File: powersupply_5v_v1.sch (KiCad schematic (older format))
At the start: 100 parts, among them T1 TRANSFO2, U1 LM7805, U2 LM7905

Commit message: annoated schematic and added labels
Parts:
- removed C1, C2, C3, C4: 1000uF, symbol CP
- removed C5, C6: 0.01uF, symbol C_Small
- removed C7, C8: 1.0uF, symbol C_Small
- removed C? (x8): C_Small, symbol C_Small
- removed C? (x2): 2200uF, symbol CP
- removed C? (x4): 10nF, symbol C_Small
- removed C? (x4): 100nF, symbol C_Small
- removed C? (x2): 470uF, symbol CP
- removed D? (x8): D, symbol D
- removed D? (x4): 1N4008, symbol D
- removed D? (x2): TVS, symbol TVS
- removed D? (x2): LED, symbol LED
- removed F? (x4): FUSE, symbol FUSE
- removed P? (x4): CONN_01X02, symbol CONN_01X02
- removed R? (x6): R, symbol R
- removed T? (x2): TRANSFO, symbol TRANSFO
- removed U1: LM7805, symbol LM7805
- removed U2: LM7905, symbol LM7905-RESCUE-powersupply_5v_v1
- removed U? (x2): 7805, symbol 7805
- added P1: AC_INPUT, symbol CONN_01X03
- added P2: POWER OUT, symbol CONN_01X03
- C1, C10, C11, C12, C13, C14, C15, C16, C17, C18, C2, C3, C4, C5, C6, C7, C8, C9: renamed from C?; MANUFACTURER_PART (none) -> empty
- D1, D2: value D -> MUR860G; MANUFACTURER_PART (none) -> empty
- D10, D5, D6, D7, D8, D9: renamed from D?; MANUFACTURER_PART (none) -> empty
- D3: renamed from D4; value D -> MUR860G; MANUFACTURER_PART (none) -> empty
- D4: renamed from D3; value D -> MUR860G; MANUFACTURER_PART (none) -> empty
- F1, F2, F3: renamed from F?; MANUFACTURER_PART (none) -> empty
- R1, R2: renamed from R?; MANUFACTURER_PART (none) -> empty
- T1: MANUFACTURER_PART (none) -> empty
- U1: renamed from U?; value 7805 -> LM7805CT/NOPB; MANUFACTURER_PART (none) -> empty
- U2: renamed from U?; value LM7905 -> LM7905CT/NOPB; MANUFACTURER_PART (none) -> empty
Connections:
- net labels removed: +5V, -5V, GND
- wire segments 339 -> 82
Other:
- note added: "References"
- note removed: "0V"
- note removed: "VCC"
- moved on the sheet: C1, C2, C3, C4, D1, D2, D3, D4, F1, T1

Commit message: bunch of stuff wasn't commited...
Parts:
- added U?: V+, symbol V+
- added U?: V-, symbol V-
- C1, C11, C12, C13, C14, C2, C3, C4: footprint (none) -> Capacitors_ThroughHole:C_Disc_D7.5_P5
- C10, C15, C16, C9: footprint (none) -> Capacitors_ThroughHole:C_Disc_D6_P5
- C17, C18: footprint (none) -> Capacitors_Elko_ThroughHole:Elko_vert_11.5x8mm_RM3.5
- C5, C6, C7, C8: footprint (none) -> w_capacitors:CP_18x16mm
- D1, D2, D3, D4: footprint (none) -> Diodes_ThroughHole:Diode_TO-220_Vertical
- D10, D5, D6, D9: footprint (none) -> Diodes_ThroughHole:Diode_DO-41_SOD81_Horizontal_RM10
- D7, D8: footprint (none) -> LEDs:LED-5MM
- F1, F2, F3: footprint (none) -> Fuse_Holders_and_Fuses:Fuseholder6x32_Horiz_Open_Schurter0031-8002
- P1, P2: footprint (none) -> w_conn_screw:mstbva_2,5%2f3-g-5,08
- R1, R2: footprint (none) -> Resistors_ThroughHole:Resistor_Horizontal_RM10mm
- T1: footprint (none) -> Transformers_SMPS_ThroughHole:ETD29_13Pin_Horizontal_EPCOS-B66359A1013T
- U1, U2: footprint (none) -> w_to:to220_std_14cw
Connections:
- net labels added: GND, GNDPWR
- wire segments 82 -> 87

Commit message: added footprint that was screwed up
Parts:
- removed U2: LM7905CT/NOPB, w_to:to220_std_14cw, symbol LM7905-RESCUE-powersupply_5v_v1
- added U?: 7905, symbol 7905
- U1: symbol 7805 -> 7805-RESCUE-powersupply_5v_v1
- gave numbers to parts that had none: 2
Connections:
- wire segments 87 -> 144
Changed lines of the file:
@@
 http://elinux.org/RPi_5V_PSU_construction
-$Comp
-L LM7905-RESCUE-powersupply_5v_v1 U2
-U 1 1 55CE5E33
-P 4850 6075
-F 0 "U2" H 5000 5880 60  0000 C CNN
-F 1 "LM7905CT/NOPB" H 4850 6275 60  0000 C CNN
-F 2 "w_to:to220_std_14cw" H 4850 6075 60  0001 C CNN
-F 3 "" H 4850 6075 60  0000 C CNN
-F 4 "empty" H 4850 6075 60  0000 C CNN "MANUFACTURER_PART"
-	1    4850 6075
-	1    0    0    -1
-$EndComp
 $Comp
 L FUSE F1
@@
 $EndComp
 $Comp
-L 7805 U1
+L 7805-RESCUE-powersupply_5v_v1 U1
 U 1 1 55CEF6E0
 P 4850 4600
@@
 References
 $Comp
-L GNDPWR #PWR?
+L GNDPWR #PWR02
 U 1 1 563A2E33
 P 1600 5395
-F 0 "#PWR?" H 1600 5195 50  0001 C CNN
+F 0 "#PWR02" H 1600 5195 50  0001 C CNN
 F 1 "GNDPWR" H 1600 5265 50  0000 C CNN
 F 2 "" H 1600 5345 60  0000 C CNN
@@
 $EndComp
 $Comp
-L V+ U?
+L V+ U3
 U 1 1 563A33A0
 P 1585 4360
-F 0 "U?" H 1555 4385 60  0000 C CNN
+F 0 "U3" H 1555 4385 60  0000 C CNN
 F 1 "V+" H 1555 4385 60  0000 C CNN
 F 2 "" H 1555 4385 60  0000 C CNN
@@
 $EndComp
 $Comp
-L V- U?
+L V- U4
 U 1 1 563A3C79
 P 1585 5870
-F 0 "U?" H 1555 5895 60  0000 C CNN
+F 0 "U4" H 1555 5895 60  0000 C CNN
 F 1 "V-" H 1555 5895 60  0000 C CNN
 F 2 "" H 1555 5895 60  0000 C CNN
@@
 $EndComp
 Wire Wire Line
-	3275 2400 4275 2400
-Wire Wire Line
-	4150 2900 4150 3050
-Wire Wire Line
-	3525 3050 4275 3050
-Wire Wire Line
-	4700 3050 4575 3050
-Wire Wire Line
-	4700 2900 4700 3600
-Wire Wire Line
-	4700 2400 4700 2600
-Wire Wire Line
-	4575 2400 5450 2400
+	3275 2400 4150 2400
+Wire Wire Line
+	4150 2400 4225 2400
+Wire Wire Line
+	4225 2400 4275 2400
+Wire Wire Line
+	4150 2900 4150 2950
+Wire Wire Line
+	4150 2950 4150 3050
+Wire Wire Line
+	3525 3050 4150 3050
+Wire Wire Line
+	4150 3050 4225 3050
+Wire Wire Line
+	4225 3050 4275 3050
+Wire Wire Line
+	4700 3050 4600 3050
+Wire Wire Line
+	4600 3050 4575 3050
+Wire Wire Line
+	4700 2900 4700 2950
+Wire Wire Line
+	4700 2950 4700 3050
+Wire Wire Line
+	4700 3050 4700 3600
+Wire Wire Line
+	4700 2400 4700 2500
+Wire Wire Line
+	4700 2500 4700 2600
+Wire Wire Line
+	4575 2400 4600 2400
+Wire Wire Line
+	4600 2400 4700 2400
+Wire Wire Line
+	4700 2400 5450 2400
 Wire Wire Line
 	4700 3600 3625 3600
@@
 	3625 3200 3625 3600
 Wire Wire Line
-	4150 2400 4150 2600
-Wire Wire Line
-	3275 2700 3275 2900
+	4150 2400 4150 2525
+Wire Wire Line
+	4150 2525 4150 2600
+Wire Wire Line
+	3275 2700 3275 2800
+Wire Wire Line
+	3275 2800 3275 2900
 Wire Wire Line
 	3275 2800 3450 2800
@@
 	1425 3100 2475 3100
 Wire Wire Line
-	1425 4550 4450 4550
-Wire Wire Line
-	1375 5350 9350 5350
-Wire Wire Line
-	2550 5125 2550 5550
+	1425 4550 1700 4550
+Wire Wire Line
+	1700 4550 2550 4550
+Wire Wire Line
+	2550 4550 2950 4550
+Wire Wire Line
+	2950 4550 3500 4550
+Wire Wire Line
+	3500 4550 3950 4550
+Wire Wire Line
+	3950 4550 4450 4550
+Wire Wire Line
+	1375 5350 1400 5350
+Wire Wire Line
+	1400 5350 1600 5350
+Wire Wire Line
+	1600 5350 2550 5350
+Wire Wire Line
+	2550 5350 2950 5350
+Wire Wire Line
+	2950 5350 3500 5350
+Wire Wire Line
+	3500 5350 3950 5350
+Wire Wire Line
+	3950 5350 4850 5350
+Wire Wire Line
+	4850 5350 6075 5350
+Wire Wire Line
+	6075 5350 6475 5350
+Wire Wire Line
+	6475 5350 6900 5350
+Wire Wire Line
+	6900 5350 7275 5350
+Wire Wire Line
+	7275 5350 7675 5350
+Wire Wire Line
+	7675 5350 8400 5350
+Wire Wire Line
+	8400 5350 9350 5350
+Wire Wire Line
+	2550 5125 2550 5350
+Wire Wire Line
+	2550 5350 2550 5550
 Wire Wire Line
 	2550 6025 2550 5850
 Connection ~ 2550 5350
 Wire Wire Line
-	2950 5125 2950 5550
+	2950 5125 2950 5350
+Wire Wire Line
+	2950 5350 2950 5550
 Connection ~ 2950 5350
 Wire Wire Line
@@
 Connection ~ 1400 5350
 Wire Wire Line
-	1425 6025 4450 6025
+	1425 6025 1580 6025
+Wire Wire Line
+	1580 6025 2550 6025
+Wire Wire Line
+	2550 6025 2950 6025
+Wire Wire Line
+	2950 6025 3500 6025
+Wire Wire Line
+	3500 6025 3950 6025
+Wire Wire Line
+	3950 6025 4450 6025
 Wire Wire Line
 	4300 2125 4225 2125
@@
 Connection ~ 3500 4550
 Wire Wire Line
-	3500 5075 3500 5600
+	3500 5075 3500 5350
+Wire Wire Line
+	3500 5350 3500 5600
 Connection ~ 3500 5350
 Wire Wire Line
@@
 	3950 4550 3950 4875
 Wire Wire Line
-	3950 5075 3950 5600
+	3950 5075 3950 5350
+Wire Wire Line
+	3950 5350 3950 5600
 Connection ~ 3950 5350
 Wire Wire Line
@@
 	6075 4850 6075 4550
 Wire Wire Line
-	5250 4550 7900 4550
+	5250 4550 6075 4550
+Wire Wire Line
+	6075 4550 6475 4550
+Wire Wire Line
+	6475 4550 6900 4550
+Wire Wire Line
+	6900 4550 7275 4550
+Wire Wire Line
+	7275 4550 7675 4550
+Wire Wire Line
+	7675 4550 7900 4550
 Wire Wire Line
 	6475 4550 6475 4850
@@
 Connection ~ 6475 4550
 Wire Wire Line
-	6075 5050 6075 5550
-Wire Wire Line
-	6475 5050 6475 5575
-Wire Wire Line
-	6900 5100 6900 5525
+	6075 5050 6075 5350
+Wire Wire Line
+	6075 5350 6075 5550
+Wire Wire Line
+	6475 5050 6475 5350
+Wire Wire Line
+	6475 5350 6475 5575
+Wire Wire Line
+	6900 5100 6900 5350
+Wire Wire Line
+	6900 5350 6900 5525
 Wire Wire Line
 	7275 4550 7275 4600
@@
 	8400 4550 8400 4775
 Wire Wire Line
-	8400 5075 8400 5550
+	8400 5075 8400 5350
+Wire Wire Line
+	8400 5350 8400 5550
 Wire Wire Line
 	8400 4550 9375 4550
@@
 	7675 5000 7675 5025
 Wire Wire Line
-	7675 5325 7675 5400
+	7675 5325 7675 5350
+Wire Wire Line
+	7675 5350 7675 5400
 Connection ~ 7675 5350
 Connection ~ 3950 6025
@@
 	8400 6025 8400 5850
 Wire Wire Line
-	5250 6025 7900 6025
+	5250 6025 6075 6025
+Wire Wire Line
+	6075 6025 6475 6025
+Wire Wire Line
+	6475 6025 6900 6025
+Wire Wire Line
+	6900 6025 7275 6025
+Wire Wire Line
+	7275 6025 7675 6025
+Wire Wire Line
+	7675 6025 7900 6025
 Wire Wire Line
 	8400 6025 9350 6025
@@
 	1725 3475 1725 3525
 Wire Wire Line
-	4850 4850 4850 5825
+	4850 4850 4850 5350
+Wire Wire Line
+	4850 5350 4850 5725
 Connection ~ 4850 5350
 Wire Wire Line
@@
 Connection ~ 5250 6025
 Connection ~ 4450 6025
-Connection ~ 4850 5825
+Connection ~ 4850 5725
 Connection ~ 4850 4850
 Connection ~ 5250 4550
@@
 Connection ~ 1580 6025
 Wire Wire Line
-	1600 5255 1600 5395
+	1600 5255 1600 5350
+Wire Wire Line
+	1600 5350 1600 5395
 Connection ~ 1600 5350
 Text Label 1615 5255 0    60   ~ 0
@@
 Wire Wire Line
 	1600 5255 1615 5255
+$Comp
+L 7905 U?
+U 1 1 563AD8EE
+P 4850 5975
+F 0 "U?" H 5000 5780 60  0000 C CNN
+F 1 "7905" H 4850 6175 60  0000 C CNN
+F 2 "" H 4850 5975 60  0000 C CNN
+F 3 "" H 4850 5975 60  0000 C CNN
+	1    4850 5975
+	1    0    0    1
+$EndComp
 $EndSCHEMATC

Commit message: added some symbol stuff
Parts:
- removed U3: V+, symbol V+
- removed U4: V-, symbol V-
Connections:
- wire segments 144 -> 90
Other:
- moved on the sheet: T1

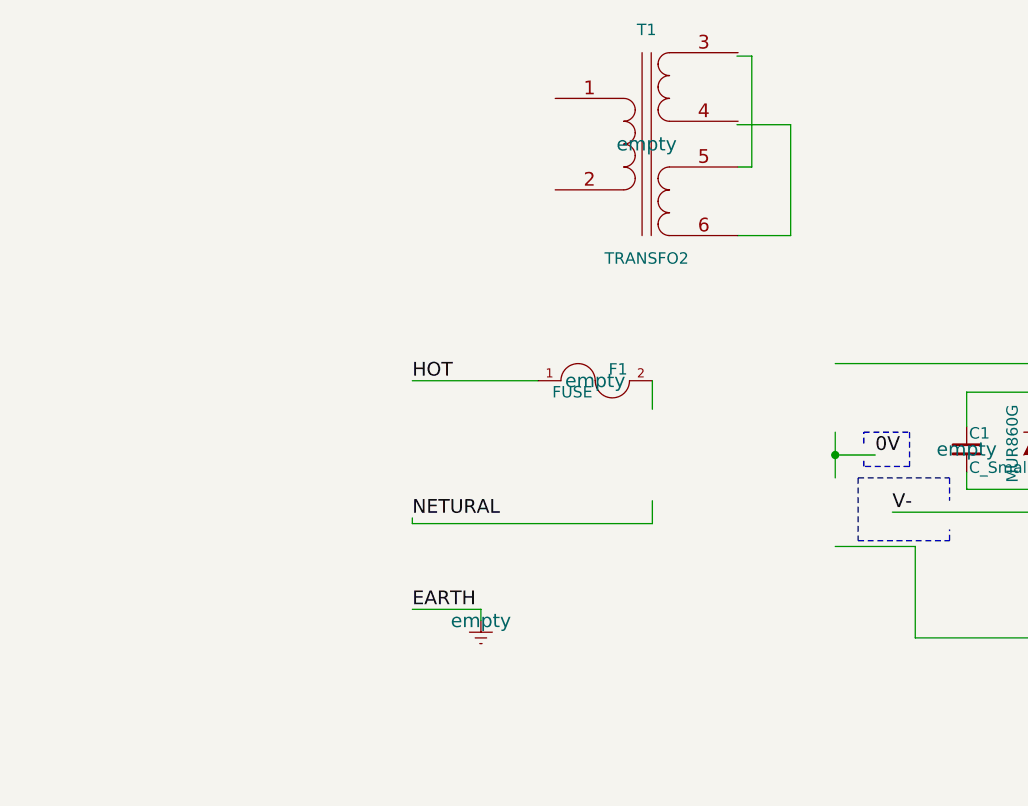
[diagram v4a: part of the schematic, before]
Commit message: trying to get this hammond transformer footprint made
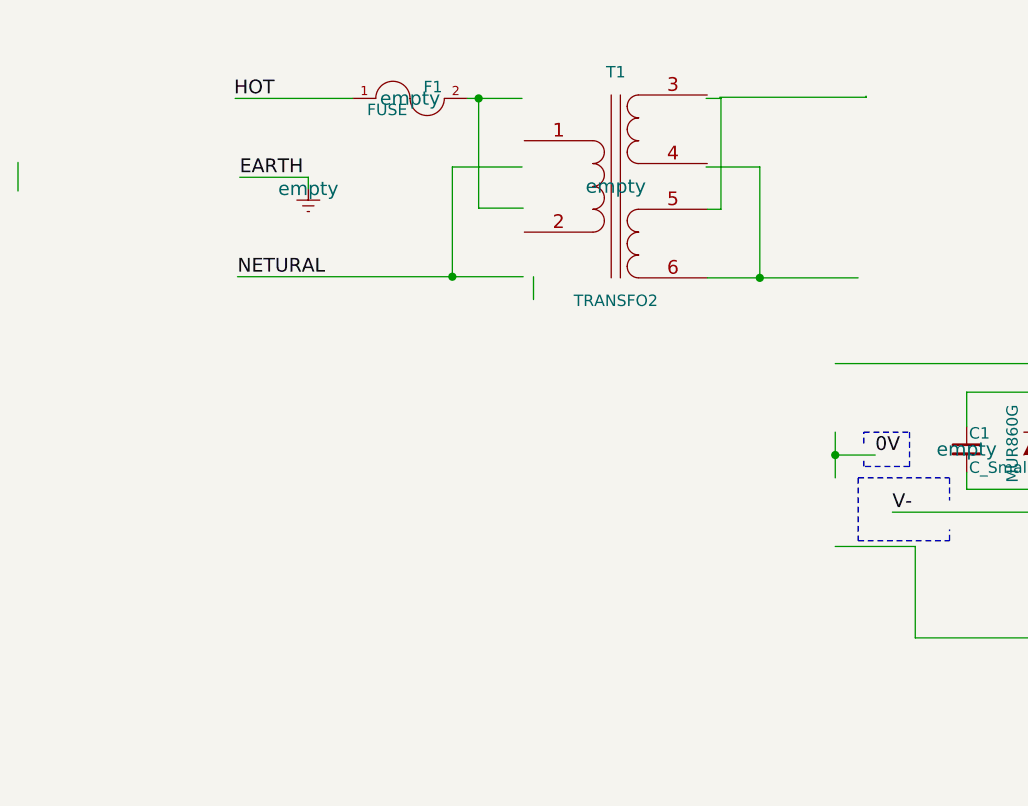
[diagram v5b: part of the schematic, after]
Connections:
- wire segments 90 -> 96
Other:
- moved on the sheet: F1, T1
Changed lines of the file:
@@
 L TRANSFO2 T1
 U 1 1 55CBB17B
-P 2450 1440
-F 0 "T1" H 2450 1940 50  0000 C CNN
-F 1 "TRANSFO2" H 2450 940 50  0000 C CNN
-F 2 "Transformers_SMPS_ThroughHole:ETD29_13Pin_Horizontal_EPCOS-B66359A1013T" H 2450 1440 60  0001 C CNN
-F 3 "" H 2450 1440 60  0000 C CNN
-F 4 "empty" H 2450 1440 60  0000 C CNN "MANUFACTURER_PART"
-	1    2450 1440
+P 2315 1625
+F 0 "T1" H 2315 2125 50  0000 C CNN
+F 1 "TRANSFO2" H 2315 1125 50  0000 C CNN
+F 2 "Transformers_SMPS_ThroughHole:ETD29_13Pin_Horizontal_EPCOS-B66359A1013T" H 2315 1625 60  0001 C CNN
+F 3 "" H 2315 1625 60  0000 C CNN
+F 4 "empty" H 2315 1625 60  0000 C CNN "MANUFACTURER_PART"
+	1    2315 1625
 	1    0    0    -1
 $EndComp
@@
 L Earth #PWR01
 U 1 1 55CD146C
-P 1725 3525
-F 0 "#PWR01" H 1725 3275 50  0001 C CNN
-F 1 "Earth" H 1725 3375 50  0001 C CNN
-F 2 "" H 1725 3525 60  0000 C CNN
-F 3 "" H 1725 3525 60  0000 C CNN
-F 4 "empty" H 1725 3525 60  0000 C CNN "MANUFACTURER_PART"
-	1    1725 3525
+P 970 1635
+F 0 "#PWR01" H 970 1385 50  0001 C CNN
+F 1 "Earth" H 970 1485 50  0001 C CNN
+F 2 "" H 970 1635 60  0000 C CNN
+F 3 "" H 970 1635 60  0000 C CNN
+F 4 "empty" H 970 1635 60  0000 C CNN "MANUFACTURER_PART"
+	1    970  1635
 	1    0    0    -1
 $EndComp
@@
 L FUSE F1
 U 1 1 55CE7C40
-P 2225 2475
-F 0 "F1" H 2325 2525 50  0000 C CNN
-F 1 "FUSE" H 2125 2425 50  0000 C CNN
-F 2 "Fuse_Holders_and_Fuses:Fuseholder6x32_Horiz_Open_Schurter0031-8002" H 2225 2475 60  0001 C CNN
-F 3 "" H 2225 2475 60  0000 C CNN
-F 4 "empty" H 2225 2475 60  0000 C CNN "MANUFACTURER_PART"
-	1    2225 2475
+P 1415 1240
+F 0 "F1" H 1515 1290 50  0000 C CNN
+F 1 "FUSE" H 1315 1190 50  0000 C CNN
+F 2 "Fuse_Holders_and_Fuses:Fuseholder6x32_Horiz_Open_Schurter0031-8002" H 1415 1240 60  0001 C CNN
+F 3 "" H 1415 1240 60  0000 C CNN
+F 4 "empty" H 1415 1240 60  0000 C CNN "MANUFACTURER_PART"
+	1    1415 1240
 	1    0    0    -1
 $EndComp
@@
 Text Label 9350 6025 0    60   ~ 0
 REG_-5V
-Text Label 1425 2475 0    60   ~ 0
+Text Label 645  1240 0    60   ~ 0
 HOT
-Text Label 1425 3075 0    60   ~ 0
+Text Label 660  2020 0    60   ~ 0
 NETURAL
-Text Label 1425 3475 0    60   ~ 0
+Text Label 670  1585 0    60   ~ 0
 EARTH
 $Comp
@@
 Connection ~ 3275 2800
 Wire Wire Line
-	2475 2475 2475 2600
-Wire Wire Line
-	1425 2475 1975 2475
-Wire Wire Line
-	2475 3100 2475 3000
-Wire Wire Line
-	1425 3100 2475 3100
+	-300 1520 -300 1645
+Wire Wire Line
+	650  1240 1165 1240
+Wire Wire Line
+	1955 2120 1955 2020
 Wire Wire Line
 	1425 4550 4450 4550
@@
 	8400 6025 9350 6025
 Wire Wire Line
-	1425 3100 1425 3075
-Wire Wire Line
-	1425 3475 1725 3475
-Wire Wire Line
-	1725 3475 1725 3525
+	670  1585 970  1585
+Wire Wire Line
+	970  1585 970  1635
 Wire Wire Line
 	4850 4850 4850 5725
@@
 	1600 5255 1615 5255
 Wire Wire Line
-	2845 1055 2910 1055
-Wire Wire Line
-	2910 1055 2910 1540
-Wire Wire Line
-	2910 1540 2850 1540
-Wire Wire Line
-	2845 1355 3080 1355
-Wire Wire Line
-	3080 1355 3080 1840
-Wire Wire Line
-	3080 1840 2850 1840
+	2710 1240 2775 1240
+Wire Wire Line
+	2775 1240 2775 1725
+Wire Wire Line
+	2945 1540 2945 2025
+Wire Wire Line
+	2715 2025 3375 2025
+Wire Wire Line
+	1665 1240 1905 1240
+Wire Wire Line
+	1715 1240 1715 1720
+Wire Wire Line
+	1715 1720 1910 1720
+Connection ~ 1715 1240
+Wire Wire Line
+	1905 1540 1600 1540
+Wire Wire Line
+	1600 1540 1600 2020
+Wire Wire Line
+	660  2020 1910 2020
+Connection ~ 1600 2020
+Wire Wire Line
+	2710 1540 2945 1540
+Wire Wire Line
+	2775 1725 2715 1725
+Connection ~ 2945 2025
+Wire Wire Line
+	2770 1235 3410 1235
+Wire Wire Line
+	3410 1235 3410 1230
 $EndSCHEMATC
